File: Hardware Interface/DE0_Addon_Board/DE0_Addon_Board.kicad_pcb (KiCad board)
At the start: 2 copper layers, 30.7 x 56.6 mm, 6 parts, among them J1 Conn_02x20_Odd_Even, J2 Conn_01x02_Male, J3 Conn_02x20_Odd_Even, U1 IS61WV25616EDBLL

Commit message: Changing daughter board to support raspberry pin connector
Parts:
- removed J2: Conn_01x02_Male, Jumper:SolderJumper-2_P1.3mm_Open_Pad1.0x1.5mm
- J3: value Conn_02x20_Odd_Even -> Raspberry PI GPIO; footprint Connector_PinHeader_2.54mm:PinHeader_2x20_P2.54mm_Vertical -> Roni Footprints:PinSocket_2x20_P2.54mm_Vertical
- moved J3 2.79 mm to (66.0, 26.4)
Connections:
- J1 pad 1: P1 -> MREQ_n
- J1 pad 20: UB_n -> M1_n
- J1 pad 21: P21 -> UB_n
- J1 pad 22: P22 -> RPI_en
- J1 pad 3: P3 -> SLTSL_n
- J1 pad 8: CE_n -> MEM_CE_n
- J3 pad 1: P1 -> +3.3V
- J3 pad 10: D1 -> A1
- J3 pad 11: unconnected-(J3-Pad11) -> IORQ_n
- J3 pad 12: GNDREF -> A3
- J3 pad 13: D11 -> WR_n
- J3 pad 14: D10 -> GNDREF
- J3 pad 15: A16 -> RD_n
- J3 pad 16: A17 -> RPI_en
- J3 pad 17: OE_n -> +3.3V
- J3 pad 18: A15 -> RPI_Ack
- J3 pad 19: LB_n -> unconnected-(J3-Pad19)
- J3 pad 2: A0 -> unconnected-(J3-Pad2)
- J3 pad 20: UB_n -> GNDREF
- J3 pad 21: P21 -> M1_n
- J3 pad 22: P22 -> A15
- J3 pad 23: A14 -> A12
- J3 pad 24: P24 -> A14
- J3 pad 25: A12 -> GNDREF
- J3 pad 29: +3.3V -> RST_n
- J3 pad 3: P3 -> MREQ_n
- J3 pad 31: D13 -> CLK
- J3 pad 32: D12 -> WAIT_n
- J3 pad 33: D15 -> A5
- J3 pad 34: D14 -> GNDREF
- J3 pad 35: A5 -> A7
- J3 pad 36: WE_n -> INT_n
- J3 pad 37: A7 -> A9
- J3 pad 39: A9 -> GNDREF
- J3 pad 4: A1 -> unconnected-(J3-Pad4)
- J3 pad 5: A2 -> SLTSL_n
- J3 pad 6: A3 -> GNDREF
- J3 pad 8: CE_n -> A0
- J3 pad 9: D0 -> GNDREF
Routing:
- net M1_n: track 0.00 -> 17.9 mm
- net CE_n: track 16.4 -> 0.00 mm
- net GNDREF: track 66.4 -> 51.4 mm
- net MREQ_n: track 0.00 -> 11.4 mm
- net SLTSL_n: track 0.00 -> 10.2 mm
- net UB_n: track 17.9 -> 8.85 mm
- net D10: track 41.9 -> 32.9 mm
- net WE_n: track 33.2 -> 24.2 mm
- net A14: track 13.6 -> 22.6 mm
- net P24: track 8.93 -> 0.00 mm
- net P22: track 8.93 -> 0.00 mm
- net D0: track 51.1 -> 42.2 mm
- net MEM_CE_n: track 15.9 -> 24.8 mm
- net P3: track 8.85 -> 0.00 mm
- net P1: track 8.85 -> 0.00 mm
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
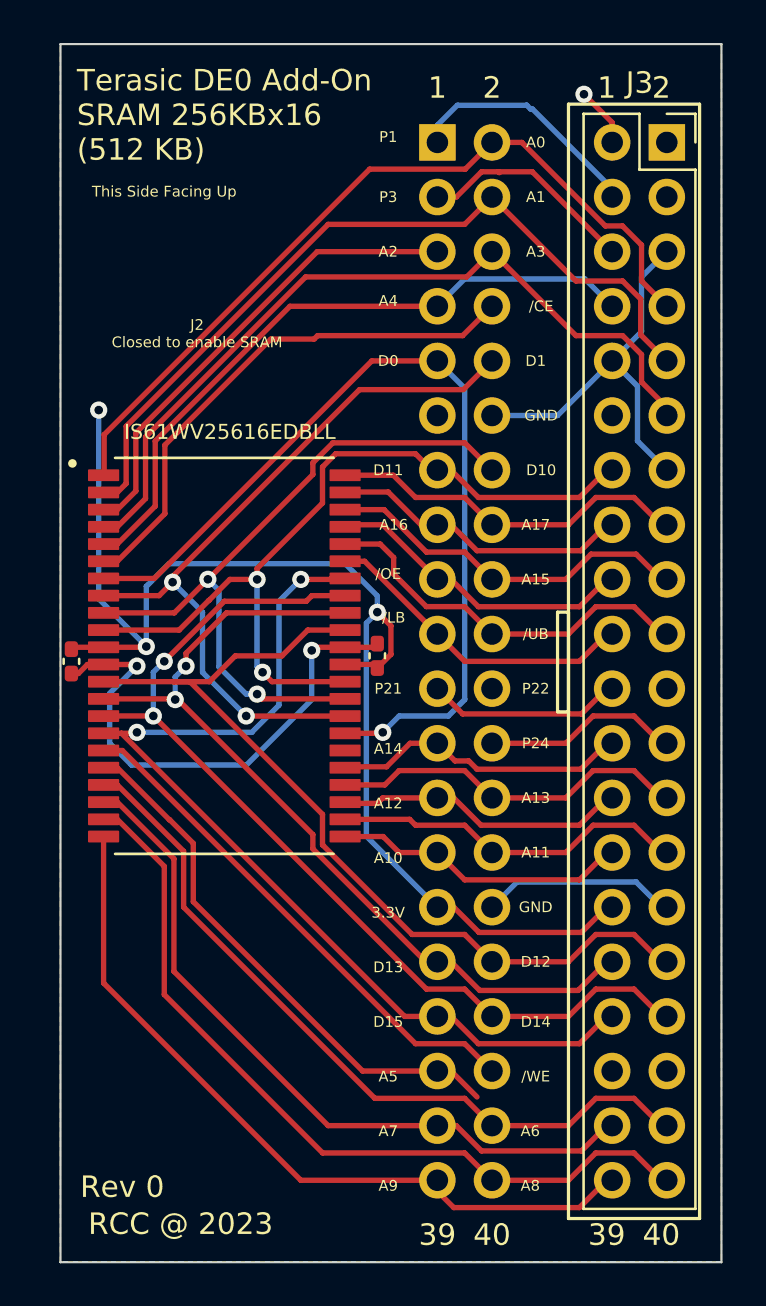
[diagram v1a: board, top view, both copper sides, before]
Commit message: Addon-board changed to support Raspberry Pi in the GPIO connector
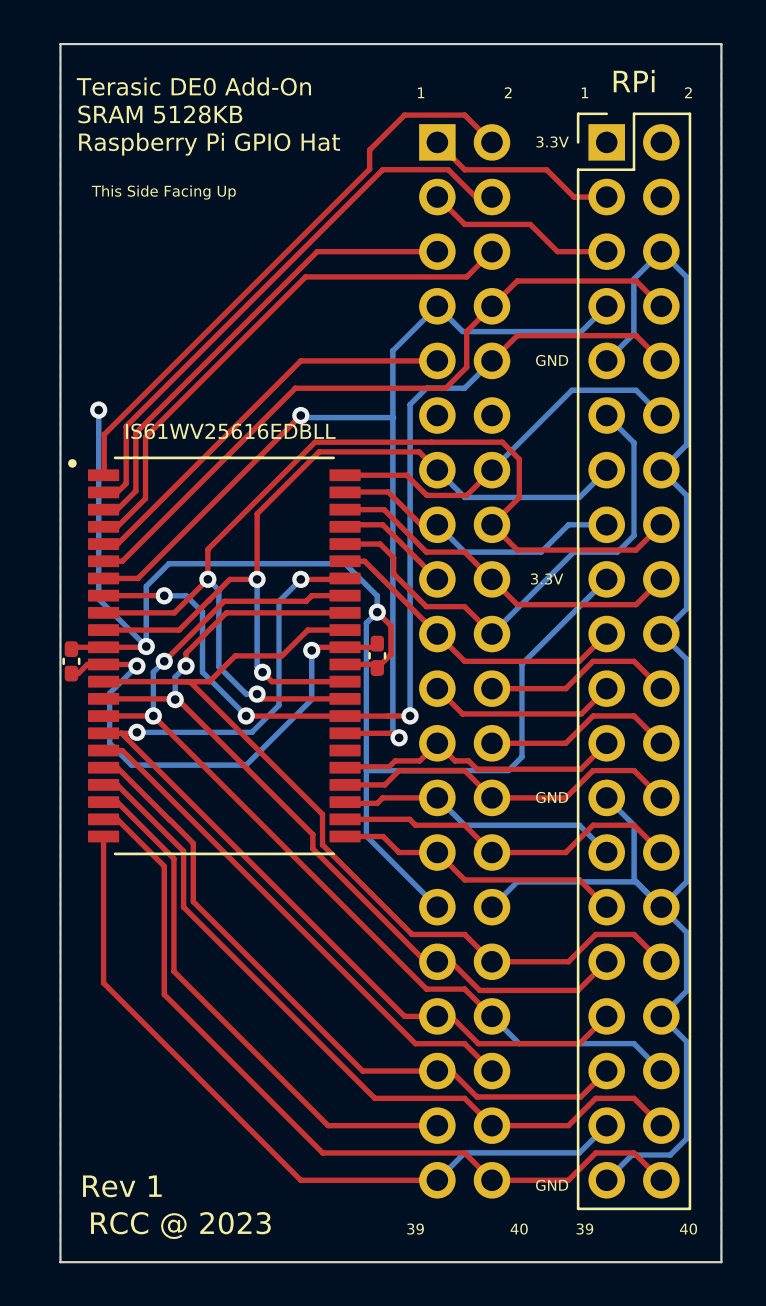
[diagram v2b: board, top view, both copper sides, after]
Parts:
- J1: value Conn_02x20_Odd_Even -> DE0/DE1 IDC Connector
- J3: value Raspberry PI GPIO -> Raspberry Pin Header; footprint Roni Footprints:PinSocket_2x20_P2.54mm_Vertical -> Connector_PinHeader_2.54mm:PinHeader_2x20_P2.54mm_Vertical
- moved J3 2.79 mm to (63.2, 26.4)
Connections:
- net MREQ_n renamed P1
- net SLTSL_n renamed P3
- net WE_n renamed P36
- J1 pad 14: D10 -> A17
- J1 pad 16: A17 -> D10
- J1 pad 19: LB_n -> IORQ_n
- J1 pad 20: M1_n -> RESET_n
- J1 pad 21: UB_n -> P21
- J1 pad 22: RPI_en -> M1_n
- J1 pad 24: P24 -> INT_n
- J1 pad 7: A4 -> D0
- J1 pad 8: MEM_CE_n -> BUSDIR_n
- J1 pad 9: D0 -> A4
- J3 pad 10: A1 -> D1
- J3 pad 11: IORQ_n -> RESET_n
- J3 pad 12: A3 -> A17
- J3 pad 13: WR_n -> D11
- J3 pad 15: RD_n -> A16
- J3 pad 16: RPI_en -> D10
- J3 pad 18: RPI_Ack -> A15
- J3 pad 19: unconnected-(J3-Pad19) -> IORQ_n
- J3 pad 21: M1_n -> P21
- J3 pad 22: A15 -> M1_n
- J3 pad 23: A12 -> A14
- J3 pad 24: A14 -> INT_n
- J3 pad 27: A10 -> A12
- J3 pad 29: RST_n -> A10
- J3 pad 31: CLK -> D13
- J3 pad 32: WAIT_n -> D12
- J3 pad 33: A5 -> D15
- J3 pad 35: A7 -> A5
- J3 pad 36: INT_n -> D14
- J3 pad 7: A4 -> D0
- J3 pad 8: A0 -> BUSDIR_n
- U1 pad 39: LB_n -> IORQ_n
- U1 pad 40: UB_n -> RESET_n
- U1 pad 6: MEM_CE_n -> BUSDIR_n
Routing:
- net GNDREF: track 51.4 -> 94.9 mm
- net BUSDIR_n: track 0.00 -> 32.8 mm
- net MEM_CE_n: track 24.8 -> 0.00 mm
- net RESET_n: track 0.00 -> 23.6 mm
- net LB_n: track 14.6 -> 0.00 mm
- net IORQ_n: track 0.00 -> 14.6 mm
- net D10: track 32.9 -> 46.9 mm
- net A3: track 37.4 -> 25.0 mm
- net A4: track 31.1 -> 19.0 mm
- net D1: track 35.0 -> 46.2 mm, vias 2 -> 3
- net A1: track 37.6 -> 26.4 mm
- net A0: track 37.8 -> 27.1 mm
- net M1_n: track 17.9 -> 8.93 mm
- net A14: track 22.6 -> 13.6 mm
- net INT_n: track 0.00 -> 8.93 mm
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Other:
- board text added: "DE0"
- board text added: "Install in DE0 GPIO 0 With This Side Facing Down"
- board text added: "RPi"
- board text added: "Rev 1"
- board text added: "Terasic DE0 Add-On SRAM 5128KB Raspberry Pi GPIO Hat"
- board text removed: "/CE"
- board text removed: "/LB"
- board text removed: "/OE"
- board text removed: "/UB"
- board text removed: "/WE"
- board text removed: "A0"
- board text removed: "A1"
- board text removed: "A10"
- board text removed: "A11"
- board text removed: "A12"
- board text removed: "A13"
- board text removed: "A14"
- board text removed: "A15"
- board text removed: "A16"
- board text removed: "A17"
- board text removed: "A2"
- board text removed: "A3"
- board text removed: "A4"
- board text removed: "A5"
- board text removed: "A6"
- board text removed: "A7"
- board text removed: "A8"
- board text removed: "A9"
- board text removed: "D0"
- board text removed: "D1"
- board text removed: "D10"
- board text removed: "D11"
- board text removed: "D12"
- board text removed: "D13"
- board text removed: "D14"
- board text removed: "D15"
- board text removed: "Install in DE0 JP1 With This Side Facing Down"
- board text removed: "J2 Closed to enable SRAM"
- board text removed: "Mount Female Conector In This Side"
- board text removed: "P1"
- board text removed: "P21"
- board text removed: "P22"
- board text removed: "P24"
- board text removed: "P3"
- board text removed: "Rev 0"
- board text removed: "Terasic DE0 Add-On SRAM 256KBx16 (512 KB)"

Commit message: Changed footprint of SRAM decoupling capacitors to SMD 0603; Updated SRAM Addon for Rev.2
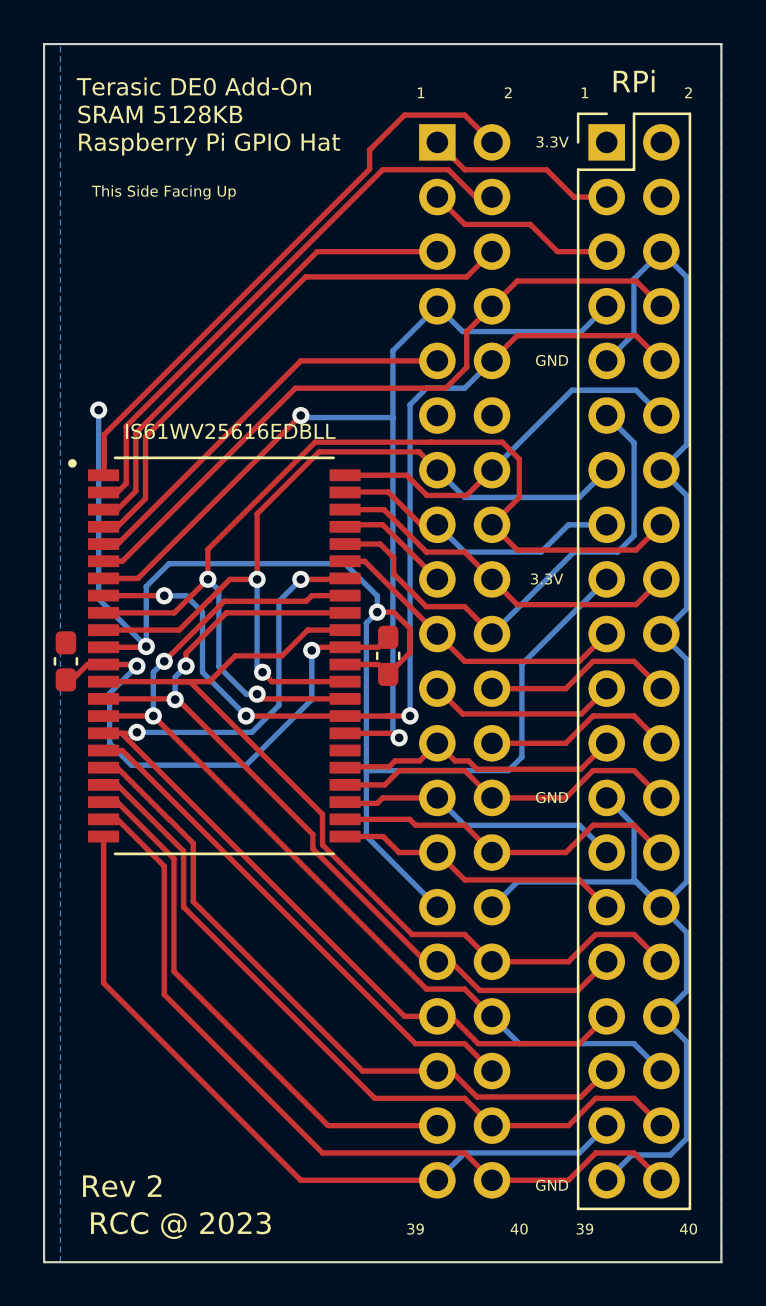
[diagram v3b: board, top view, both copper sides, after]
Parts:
- C1, C2: footprint Capacitor_SMD:C_0402_1005Metric_Pad0.74x0.62mm_HandSolder -> Capacitor_SMD:C_0603_1608Metric_Pad1.08x0.95mm_HandSolder
- J3: value Raspberry Pin Header -> Raspberry Pi Pin Header
- moved C1 0.51 mm to (53.1, 50.3)
- moved C2 0.25 mm to (38.1, 50.5)
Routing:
- net GNDREF: track 94.9 -> 96.2 mm
- net +3.3V: track 68.2 -> 69.0 mm
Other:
- board size 30.7 x 56.6 mm -> 31.5 x 56.6 mm
- board text added: "Rev 2"
- board text removed: "Rev 1"

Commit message: Updated Add-On with silk in addresses for RPI
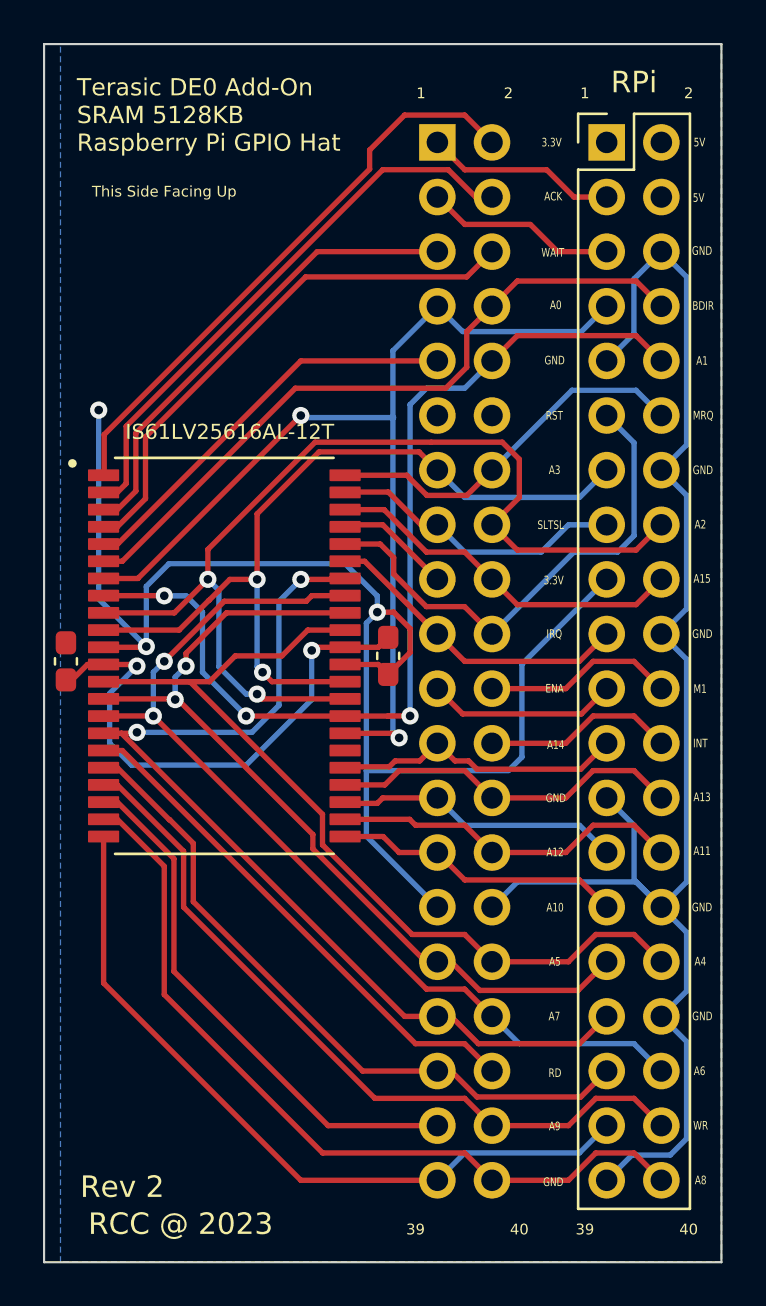
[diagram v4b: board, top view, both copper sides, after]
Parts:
- U1: value IS61WV25616EDBLL -> IS61LV25616AL-12T
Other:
- board text added: "5V"
- board text added: "A0"
- board text added: "A1"
- board text added: "A10"
- board text added: "A11"
- board text added: "A12"
- board text added: "A13"
- board text added: "A14"
- board text added: "A15"
- board text added: "A2"
- board text added: "A3"
- board text added: "A4"
- board text added: "A5"
- board text added: "A6"
- board text added: "A7"
- board text added: "A8"
- board text added: "A9"
- board text added: "ACK"
- board text added: "BDIR"
- board text added: "ENA"
- board text added: "INT"
- board text added: "IRQ"
- board text added: "M1"
- board text added: "MRQ"
- board text added: "RD"
- board text added: "RST"
- board text added: "SLTSL"
- board text added: "WAIT"
- board text added: "WR"
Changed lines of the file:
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@@
   (title_block
     (title "Terasic DE0 SRAM & Raspberry Pi Add-On")
-    (date "2023-02-16")
+    (date "2023-02-21")
     (rev "2")
   )
@@
       (effects (font (size 0.7 0.7) (thickness 0.15)))
     )
-    (fp_text value "IS61WV25616EDBLL" (at 0.254 -10.414) (layer "F.SilkS")
+    (fp_text value "IS61LV25616AL-12T" (at 0.254 -10.414) (layer "F.SilkS")
       (effects (font (size 0.7 0.7) (thickness 0.15)))
     )
@@
     (effects (font (size 1 1) (thickness 0.15)) (justify mirror))
   )
-  (gr_text "GND" (at 60.706 74.93) (layer "F.SilkS")
-    (effects (font (size 0.5 0.5) (thickness 0.1)))
+  (gr_text "GND" (at 60.760341 74.759289) (layer "F.SilkS")
+    (effects (font (size 0.4 0.3) (thickness 0.075)))
+  )
+  (gr_text "A12" (at 60.843221 59.423652) (layer "F.SilkS")
+    (effects (font (size 0.4 0.3) (thickness 0.075)))
+  )
+  (gr_text "A11" (at 67.678856 59.364256) (layer "F.SilkS")
+    (effects (font (size 0.4 0.3) (thickness 0.075)))
+  )
+  (gr_text "A4" (at 67.600227 64.501335) (layer "F.SilkS")
+    (effects (font (size 0.4 0.3) (thickness 0.075)))
   )
   (gr_text "39" (at 62.23 76.962) (layer "F.SilkS")
     (effects (font (size 0.5 0.5) (thickness 0.125)))
   )
-  (gr_text "3.3V" (at 60.452 46.736) (layer "F.SilkS")
-    (effects (font (size 0.5 0.5) (thickness 0.1)))
-  )
-  (gr_text "GND" (at 60.706 56.896) (layer "F.SilkS")
-    (effects (font (size 0.5 0.5) (thickness 0.1)))
+  (gr_text "BDIR" (at 67.731275 34.015651) (layer "F.SilkS")
+    (effects (font (size 0.4 0.3) (thickness 0.075)))
+  )
+  (gr_text "A2" (at 67.600227 44.184972) (layer "F.SilkS")
+    (effects (font (size 0.4 0.3) (thickness 0.075)))
+  )
+  (gr_text "GND" (at 60.823943 36.55206) (layer "F.SilkS")
+    (effects (font (size 0.4 0.3) (thickness 0.075)))
+  )
+  (gr_text "RD" (at 60.838969 69.687733) (layer "F.SilkS")
+    (effects (font (size 0.4 0.3) (thickness 0.075)))
+  )
+  (gr_text "A8" (at 67.613332 74.675243) (layer "F.SilkS")
+    (effects (font (size 0.4 0.3) (thickness 0.075)))
+  )
+  (gr_text "SLTSL" (at 60.640476 44.20526) (layer "F.SilkS")
+    (effects (font (size 0.4 0.3) (thickness 0.075)))
+  )
+  (gr_text "3.3V" (at 60.781541 46.779506) (layer "F.SilkS")
+    (effects (font (size 0.4 0.3) (thickness 0.075)))
+  )
+  (gr_text "A5" (at 60.838969 64.511339) (layer "F.SilkS")
+    (effects (font (size 0.4 0.3) (thickness 0.075)))
+  )
+  (gr_text "A0" (at 60.875605 33.979707) (layer "F.SilkS")
+    (effects (font (size 0.4 0.3) (thickness 0.075)))
+  )
+  (gr_text "A9" (at 60.825865 72.164539) (layer "F.SilkS")
+    (effects (font (size 0.4 0.3) (thickness 0.075)))
+  )
+  (gr_text "GND" (at 60.882536 56.907531) (layer "F.SilkS")
+    (effects (font (size 0.4 0.3) (thickness 0.075)))
   )
   (gr_text "40" (at 59.182 76.962) (layer "F.SilkS")
     (effects (font (size 0.5 0.5) (thickness 0.125)))
   )
+  (gr_text "5V" (at 67.521598 28.994549) (layer "F.SilkS")
+    (effects (font (size 0.4 0.3) (thickness 0.075)))
+  )
+  (gr_text "A15" (at 67.678856 46.705679) (layer "F.SilkS")
+    (effects (font (size 0.4 0.3) (thickness 0.075)))
+  )
   (gr_text "1" (at 54.61 24.13) (layer "F.SilkS")
     (effects (font (size 0.5 0.5) (thickness 0.125)))
   )
+  (gr_text "RST" (at 60.810838 39.1206) (layer "F.SilkS")
+    (effects (font (size 0.4 0.3) (thickness 0.075)))
+  )
   (gr_text "2" (at 67.056 24.13) (layer "F.SilkS")
     (effects (font (size 0.5 0.5) (thickness 0.125)))
   )
-  (gr_text "3.3V" (at 60.706 26.416) (layer "F.SilkS")
-    (effects (font (size 0.5 0.5) (thickness 0.1)))
+  (gr_text "3.3V" (at 60.684799 26.417165) (layer "F.SilkS")
+    (effects (font (size 0.4 0.3) (thickness 0.075)))
   )
   (gr_text "Terasic DE0 Add-On\nSRAM 5128KB \nRaspberry Pi GPIO Hat\n" (at 38.608 25.146) (layer "F.SilkS")
     (effects (font (size 0.8 0.8) (thickness 0.15)) (justify left))
   )
+  (gr_text "IRQ" (at 60.807751 49.269417) (layer "F.SilkS")
+    (effects (font (size 0.4 0.3) (thickness 0.075)))
+  )
+  (gr_text "ACK" (at 60.757662 28.927808) (layer "F.SilkS")
+    (effects (font (size 0.4 0.3) (thickness 0.075)))
+  )
   (gr_text "RCC @ 2023" (at 43.434 76.708) (layer "F.SilkS")
     (effects (font (size 1 1) (thickness 0.15)))
@@
     (effects (font (size 0.5 0.5) (thickness 0.125)))
   )
-  (gr_text "GND" (at 60.706 36.576) (layer "F.SilkS")
-    (effects (font (size 0.5 0.5) (thickness 0.1)))
+  (gr_text "GND" (at 67.678856 31.458251) (layer "F.SilkS")
+    (effects (font (size 0.4 0.3) (thickness 0.075)))
+  )
+  (gr_text "A6" (at 67.564 69.596) (layer "F.SilkS")
+    (effects (font (size 0.4 0.3) (thickness 0.075)))
+  )
+  (gr_text "ENA" (at 60.820856 51.811747) (layer "F.SilkS")
+    (effects (font (size 0.4 0.3) (thickness 0.075)))
+  )
+  (gr_text "A1" (at 67.678856 36.571086) (layer "F.SilkS")
+    (effects (font (size 0.4 0.3) (thickness 0.075)))
   )
   (gr_text "Rev 2" (at 40.719349 74.986192) (layer "F.SilkS")
     (effects (font (size 1 1) (thickness 0.15)))
   )
+  (gr_text "5V" (at 67.560913 26.412905) (layer "F.SilkS")
+    (effects (font (size 0.4 0.3) (thickness 0.075)))
+  )
+  (gr_text "M1" (at 67.587122 51.829654) (layer "F.SilkS")
+    (effects (font (size 0.4 0.3) (thickness 0.075)))
+  )
   (gr_text "This Side Facing Up" (at 42.672 28.702) (layer "F.SilkS")
     (effects (font (size 0.5 0.5) (thickness 0.125)))
   )
+  (gr_text "WR" (at 67.613332 72.132913) (layer "F.SilkS")
+    (effects (font (size 0.4 0.3) (thickness 0.075)))
+  )
   (gr_text "40" (at 67.056 76.962) (layer "F.SilkS")
     (effects (font (size 0.5 0.5) (thickness 0.125)))
   )
+  (gr_text "A13" (at 67.678856 56.86124) (layer "F.SilkS")
+    (effects (font (size 0.4 0.3) (thickness 0.075)))
+  )
+  (gr_text "WAIT" (at 60.738005 31.542215) (layer "F.SilkS")
+    (effects (font (size 0.4 0.3) (thickness 0.075)))
+  )
+  (gr_text "GND" (at 67.69196 49.274219) (layer "F.SilkS")
+    (effects (font (size 0.4 0.3) (thickness 0.075)))
+  )
   (gr_text "1" (at 62.23 24.13) (layer "F.SilkS")
     (effects (font (size 0.5 0.5) (thickness 0.125)))
+  )
+  (gr_text "A14" (at 60.873275 54.432706) (layer "F.SilkS")
+    (effects (font (size 0.4 0.3) (thickness 0.075)))
+  )
+  (gr_text "A7" (at 60.81276 67.053669) (layer "F.SilkS")
+    (effects (font (size 0.4 0.3) (thickness 0.075)))
+  )
+  (gr_text "GND" (at 67.678856 61.985215) (layer "F.SilkS")
+    (effects (font (size 0.4 0.3) (thickness 0.075)))
+  )
+  (gr_text "A10" (at 60.843221 61.992191) (layer "F.SilkS")
+    (effects (font (size 0.4 0.3) (thickness 0.075)))
   )
   (gr_text "RPi" (at 64.516 23.622) (layer "F.SilkS")
     (effects (font (size 1 1) (thickness 0.15)))
   )
+  (gr_text "MRQ" (at 67.731275 39.113416) (layer "F.SilkS")
+    (effects (font (size 0.4 0.3) (thickness 0.075)))
+  )
+  (gr_text "A3" (at 60.823943 41.649826) (layer "F.SilkS")
+    (effects (font (size 0.4 0.3) (thickness 0.075)))
+  )
+  (gr_text "GND" (at 67.71817 41.655747) (layer "F.SilkS")
+    (effects (font (size 0.4 0.3) (thickness 0.075)))
+  )
+  (gr_text "GND" (at 67.69196 67.048252) (layer "F.SilkS")
+    (effects (font (size 0.4 0.3) (thickness 0.075)))
+  )
   (gr_text "2" (at 58.674 24.13) (layer "F.SilkS")
     (effects (font (size 0.5 0.5) (thickness 0.125)))
   )
+  (gr_text "INT" (at 67.600227 54.358879) (layer "F.SilkS")
+    (effects (font (size 0.4 0.3) (thickness 0.075)))
+  )
   (segment (start 56.646278 27.690278) (end 60.456278 27.690278) (width 0.25) (layer "F.Cu") (net 1))
